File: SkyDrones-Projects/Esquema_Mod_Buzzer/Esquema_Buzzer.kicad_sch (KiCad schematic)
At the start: 13 parts, among them J1 Conn_01x02_Pin, J2 Conn_01x03_Pin, Q1 BC337, U1 PC817, U2 MT3608

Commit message: [ADD] atualização do SCHEMA
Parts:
- added C3: FCC0805X106K350FT 10uF, Capacitor_SMD:CP_Elec_3x5.3, symbol Device:C
- added C4: PHV1JVB680MC10FVTSWP 68uF, symbol Device:C_Polarized
- C1: renamed from C2; value 22uF -> CL10A226MQ8NRNC 22uF
- C2: renamed from C1; value 100uf -> CL31A107MQHNNNE 100uF
- J1: value Conn_01x02_Pin -> X30-M
- L1: value 10uH -> 22uH
- renumbered R2 to R1, R3 to R2, R1 to R3, U2 to U1, U1 to U2
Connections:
- net GND: now also C3.2, C4.2
- net 5V: now reaches C1.1, J1.2 (Pin_2), L1.1, U1.4 (EN), U1.5 (IN), U2.4
- net 5V: now also J2.2 (Pin_2)
- net at BZ1.1 (+), C2.1, D1.1 (K)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: now also C3.1, C4.1
- no-connect marks 1 -> 0
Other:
- moved on the sheet: BZ1, C1, C2, D1, J1, J2, L1, Q1, R1, R2, R3, U1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

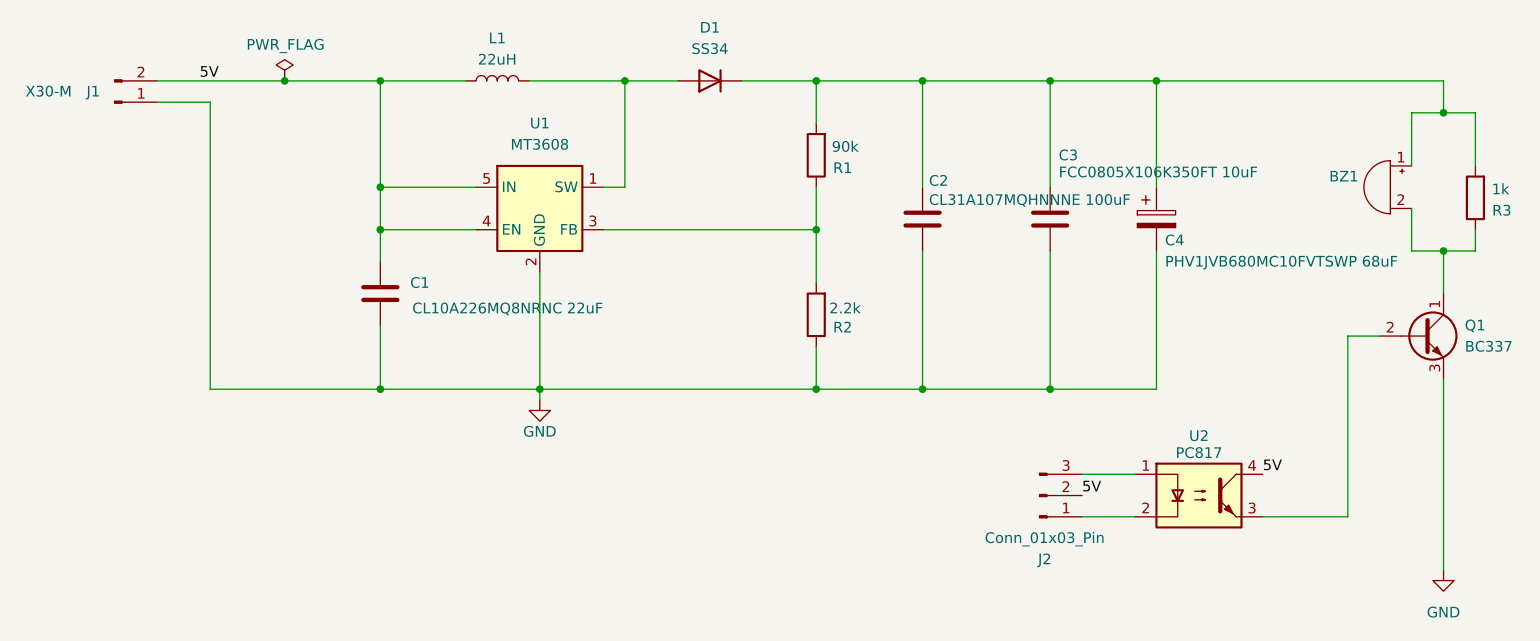
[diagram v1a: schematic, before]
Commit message: [ADD] new project and upgrade
Upgrade - buzzer SD017
Nem Project - EC01 Sensor Universal
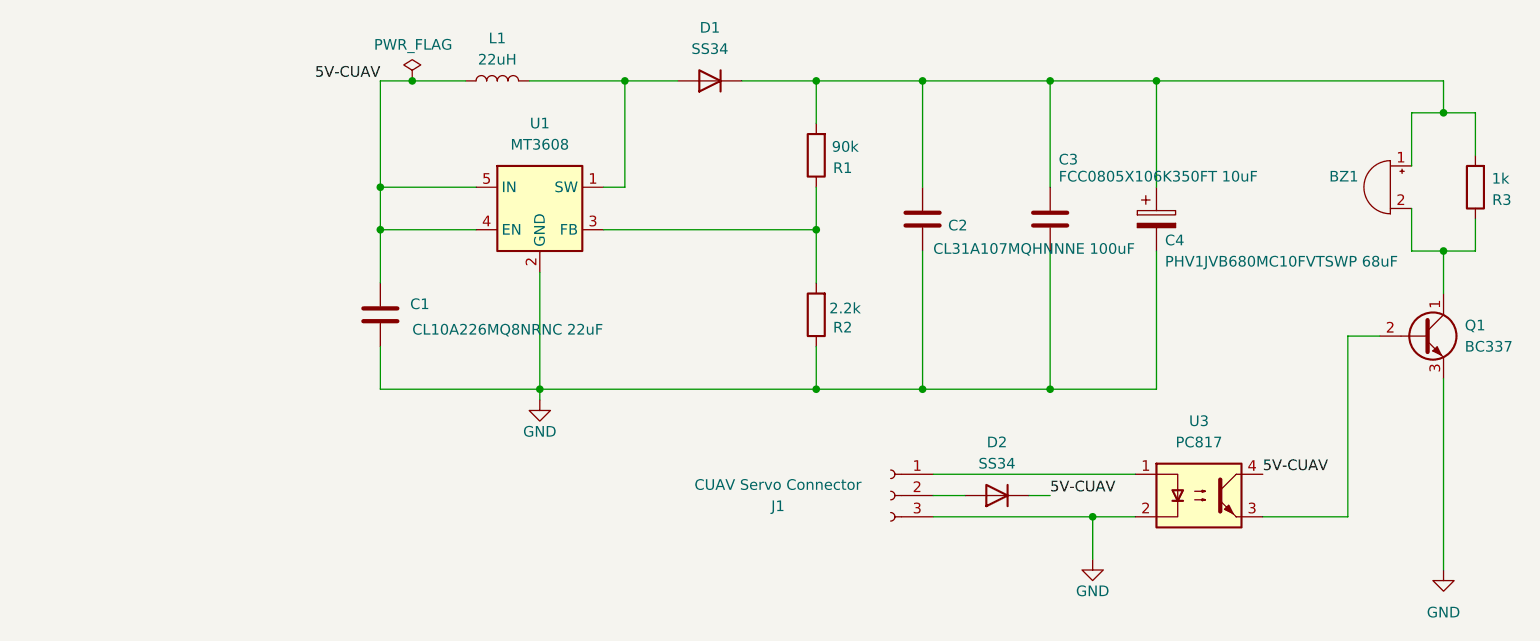
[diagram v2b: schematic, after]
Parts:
- removed J1: X30-M, Amass:AMASS_XT30PW-M_1x02_P2.50mm_Horizontal, symbol Connector:Conn_01x02_Pin
- removed J2: Conn_01x03_Pin, Connector_PinHeader_2.54mm:PinHeader_1x03_P2.54mm_Horizontal, symbol Connector:Conn_01x03_Pin
- removed U2: PC817, Package_DIP:DIP-4_W7.62mm, symbol Isolator:PC817
- added D2: SS34, Diode_SMD:D_SMA, symbol Device:D
- added J1: CUAV Servo Connector, Connector_PinSocket_2.00mm:PinSocket_1x03_P2.00mm_Vertical, symbol Connector:Conn_01x03_Socket
- added U3: PC817, Package_DIP:DIP-4_W7.62mm_SMDSocket_SmallPads, symbol Isolator:PC817
- C1: footprint Capacitor_SMD:CP_Elec_3x5.3 -> Capacitor_SMD:C_0603_1608Metric
- C2: footprint Capacitor_SMD:CP_Elec_3x5.3 -> Capacitor_SMD:C_1206_3216Metric
- C3: footprint Capacitor_SMD:CP_Elec_3x5.3 -> Capacitor_SMD:C_0805_2012Metric
- C4: footprint (none) -> Capacitor_SMD:CP_Elec_6.3x7.7
- D1: footprint Diode_SMD:D_2114_3652Metric_Pad1.85x3.75mm_HandSolder -> Diode_SMD:D_SMA
- Q1: footprint Package_TO_SOT_THT:TO-92_Inline -> Package_TO_SOT_SMD:SOT-223
- R3: footprint Resistor_THT:R_Axial_DIN0204_L3.6mm_D1.6mm_P5.08mm_Horizontal -> Resistor_SMD:R_0402_1005Metric
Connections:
- net GND: now also J1.3 (Pin_3), U3.2
- net at Q1.2 (B): now also U3.3
- net 5V renamed 5V-CUAV
- net 5V-CUAV: now also D2.1 (K), U3.4
- new net: J1.1 (Pin_1), U3.1
- new net: D2.2 (A), J1.2 (Pin_2)
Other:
- moved on the sheet: C1, R3
